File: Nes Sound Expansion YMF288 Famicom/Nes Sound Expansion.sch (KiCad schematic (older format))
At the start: 31 parts, among them J1 OUT, J2 EXP 1-30, J3 EXP 1-30, J4 31-60, J8 EXP 25-48, J9 EXP 1-24, U1 74LS139, U10 74LS257, U2 74LS132, U6 74LS174, U7 74LS174, U8 74LS257, U9 74LS257, X1 CXO_DIP8

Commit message: changed reset circuit
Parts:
- removed D1: 1N4148, Diode_SMD:D_MiniMELF, symbol Diode:1N4148
- added R4: 1k, Resistor_SMD:R_0805_2012Metric_Pad1.20x1.40mm_HandSolder, symbol Device:R
- C1: value 68pF -> 10uF
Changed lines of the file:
@@
 P 6750 4150
 F 0 "C1" V 7002 4150 50  0000 C CNN
-F 1 "68pF" V 6911 4150 50  0000 C CNN
+F 1 "10uF" V 6911 4150 50  0000 C CNN
 F 2 "Capacitor_SMD:C_0504_1310Metric_Pad0.83x1.28mm_HandSolder" H 6788 4000 50  0001 C CNN
 F 3 "~" H 6750 4150 50  0001 C CNN
@@
 Wire Wire Line
 	6050 6350 6050 6450
-$Comp
-L Diode:1N4148 D1
-U 1 1 5F812481
-P 7300 4150
-F 0 "D1" H 7300 4367 50  0000 C CNN
-F 1 "1N4148" H 7300 4276 50  0000 C CNN
-F 2 "Diode_SMD:D_MiniMELF" H 7300 3975 50  0001 C CNN
-F 3 "https://assets.nexperia.com/documents/data-sheet/1N4148_1N4448.pdf" H 7300 4150 50  0001 C CNN
-	1    7300 4150
-	-1   0    0    1
-$EndComp
 $Comp
 L power:+5V #PWR05
@@
 Text GLabel 2300 1850 2    50   Input ~ 0
 A9
+$Comp
+L Device:R R4
+U 1 1 6086CC35
+P 7300 4150
+F 0 "R4" V 7093 4150 50  0000 C CNN
+F 1 "1k" V 7184 4150 50  0000 C CNN
+F 2 "Resistor_SMD:R_0805_2012Metric_Pad1.20x1.40mm_HandSolder" V 7230 4150 50  0001 C CNN
+F 3 "~" H 7300 4150 50  0001 C CNN
+	1    7300 4150
+	0    1    1    0
+$EndComp
 $EndSCHEMATC

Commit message: Updated mixing on the Famicom version
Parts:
- added R6: 3k, Resistor_SMD:R_0805_2012Metric_Pad1.20x1.40mm_HandSolder, symbol Device:R
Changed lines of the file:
@@
 $EndComp
 Text GLabel 10750 3050 2    50   Input ~ 0
-Aud
+AudIn
 Text GLabel 6550 1150 0    50   Input ~ 0
 Addr_R-W
@@
 	1    0    0    -1
 $EndComp
-Text GLabel 3950 2650 2    50   Input ~ 0
+Text GLabel 4250 2650 2    50   Input ~ 0
 AudIn
 $Comp
@@
 	0    1    1    0
 $EndComp
+$Comp
+L Device:R R6
+U 1 1 609556A0
+P 4100 2650
+F 0 "R6" V 3893 2650 50  0000 C CNN
+F 1 "3k" V 3984 2650 50  0000 C CNN
+F 2 "Resistor_SMD:R_0805_2012Metric_Pad1.20x1.40mm_HandSolder" V 4030 2650 50  0001 C CNN
+F 3 "~" H 4100 2650 50  0001 C CNN
+	1    4100 2650
+	0    1    1    0
+$EndComp

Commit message: Added IRQ from the YMF288
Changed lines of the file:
@@
 	0    1    1    0
 $EndComp
+Text GLabel 7550 3400 2    50   Input ~ 0
+IRQ
 $EndSCHEMATC

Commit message: Redesigned to fit a Famicom MMC cart and updated readme
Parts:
- removed R1, R2, R3: 1k, Resistor_SMD:R_0805_2012Metric_Pad1.20x1.40mm_HandSolder, symbol Device:R
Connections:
- wire segments 69 -> 70
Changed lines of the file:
@@
 	0    -1   -1   0
-$EndComp
-$Comp
-L Device:R R1
-U 1 1 605439A0
-P 8250 2600
-F 0 "R1" V 8043 2600 50  0000 C CNN
-F 1 "1k" V 8134 2600 50  0000 C CNN
-F 2 "Resistor_SMD:R_0805_2012Metric_Pad1.20x1.40mm_HandSolder" V 8180 2600 50  0001 C CNN
-F 3 "~" H 8250 2600 50  0001 C CNN
-	1    8250 2600
-	0    1    1    0
-$EndComp
-$Comp
-L Device:R R2
-U 1 1 60544211
-P 8250 2700
-F 0 "R2" V 8043 2700 50  0000 C CNN
-F 1 "1k" V 8134 2700 50  0000 C CNN
-F 2 "Resistor_SMD:R_0805_2012Metric_Pad1.20x1.40mm_HandSolder" V 8180 2700 50  0001 C CNN
-F 3 "~" H 8250 2700 50  0001 C CNN
-	1    8250 2700
-	0    1    1    0
-$EndComp
-$Comp
-L Device:R R3
-U 1 1 60544656
-P 8250 2800
-F 0 "R3" V 8043 2800 50  0000 C CNN
-F 1 "1k" V 8134 2800 50  0000 C CNN
-F 2 "Resistor_SMD:R_0805_2012Metric_Pad1.20x1.40mm_HandSolder" V 8180 2800 50  0001 C CNN
-F 3 "~" H 8250 2800 50  0001 C CNN
-	1    8250 2800
-	0    1    1    0
 $EndComp
 Wire Wire Line
@@
 	8100 2300 7550 2300
 Wire Wire Line
-	8100 2700 8000 2700
-Wire Wire Line
 	8000 2700 8000 2500
 Wire Wire Line
 	8000 2500 7550 2500
-Wire Wire Line
-	8100 2800 7900 2800
 Wire Wire Line
 	7900 2800 7900 2600
@@
 Text GLabel 7550 3400 2    50   Input ~ 0
 IRQ
+Wire Wire Line
+	8100 2600 8400 2600
+Wire Wire Line
+	8000 2700 8400 2700
+Wire Wire Line
+	7900 2800 8400 2800
 $EndSCHEMATC

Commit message: Added amplification for both famicom and nes model
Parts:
- added C7: 68pF, Capacitor_SMD:C_0504_1310Metric_Pad0.83x1.28mm_HandSolder, symbol Device:C
- added C8, C9: 10uF, Capacitor_SMD:C_0504_1310Metric_Pad0.83x1.28mm_HandSolder, symbol Device:C
- added R1, R2, R7: 47k, Resistor_SMD:R_0805_2012Metric_Pad1.20x1.40mm_HandSolder, symbol Device:R
- added R3: 4.7k, Resistor_SMD:R_0805_2012Metric_Pad1.20x1.40mm_HandSolder, symbol Device:R
- added R9: 1k, Resistor_SMD:R_0805_2012Metric_Pad1.20x1.40mm_HandSolder, symbol Device:R
- added U3: LM321, Package_TO_SOT_SMD:SOT-23-5, symbol Amplifier_Operational:LM321
- C6: value 1uF -> 10uF
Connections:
- wire segments 70 -> 74
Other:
- moved on the sheet: C1, C2, C6, J1, J2, J3, J4, J8, J9, R4, R5, R6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

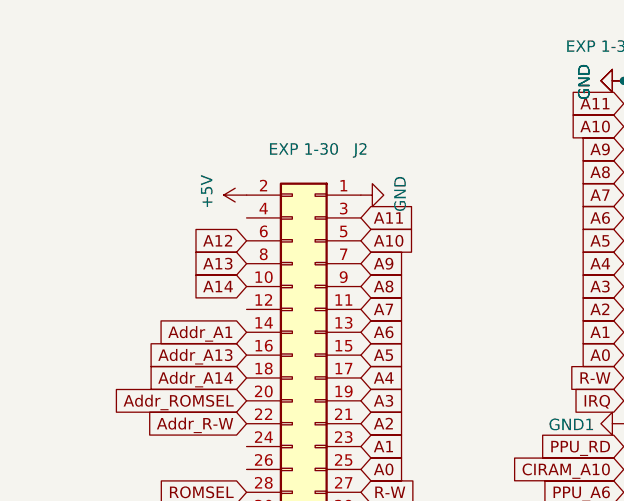
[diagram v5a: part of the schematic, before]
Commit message: Added M2 to the addressing circuit and famicom daughterboard connector
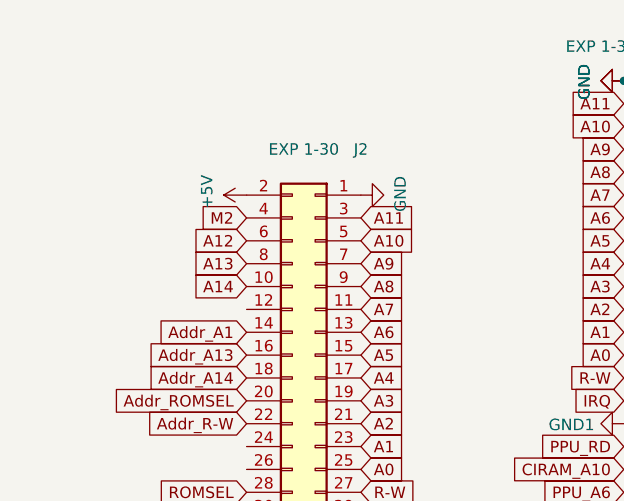
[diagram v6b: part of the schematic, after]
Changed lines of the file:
@@
 	1    0    0    -1
 $EndComp
+Text GLabel 1550 1500 0    50   Input ~ 0
+M2
 $EndSCHEMATC
